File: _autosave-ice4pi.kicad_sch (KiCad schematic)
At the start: 32 parts, among them J1 Conn_02x03, J2 Raspberry_Pi_2_3, J3 USB_C_Receptacle_USB2.0, J5 RJ45_Abracon_ARJP11A-MASA-B-A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, U1 ENC28J60x-SS, U2 DSC1001DE1-025.0000, U3 TPS2375-1

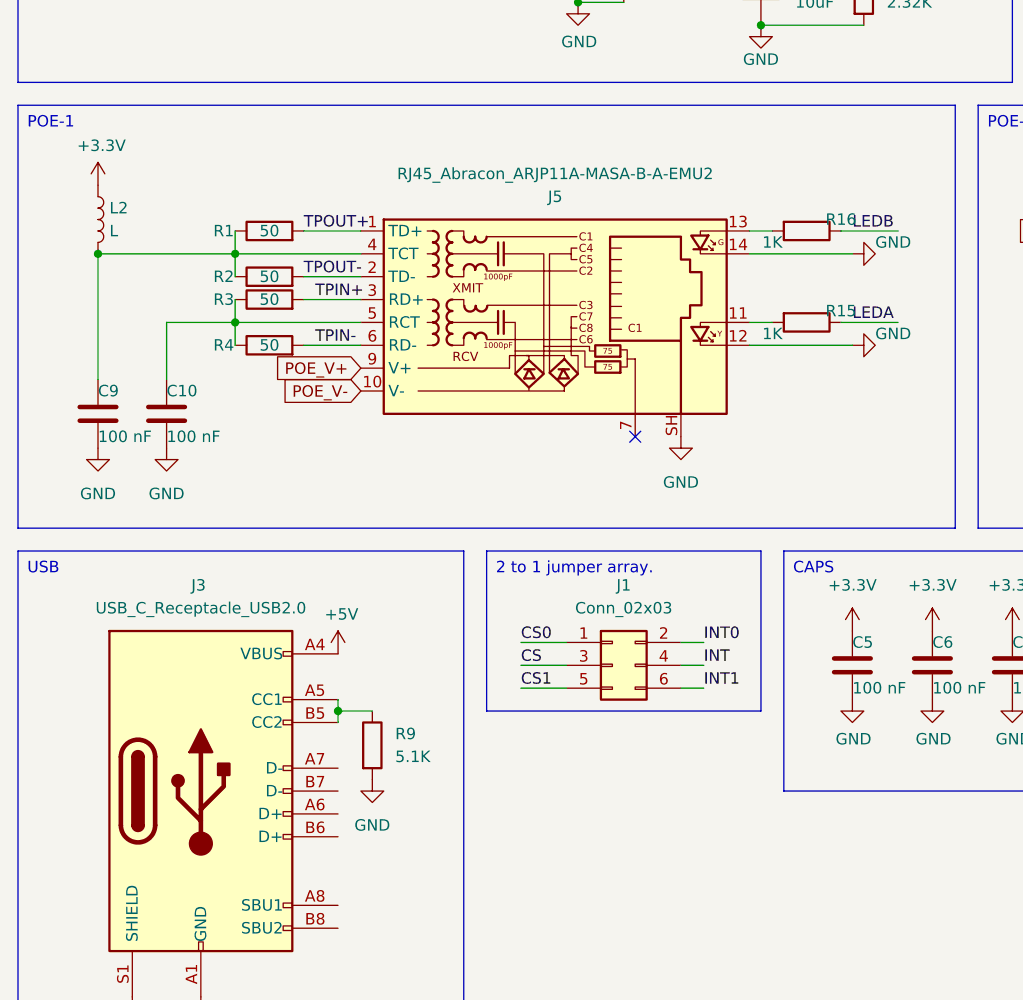
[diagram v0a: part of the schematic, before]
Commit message: feat: pos.csv
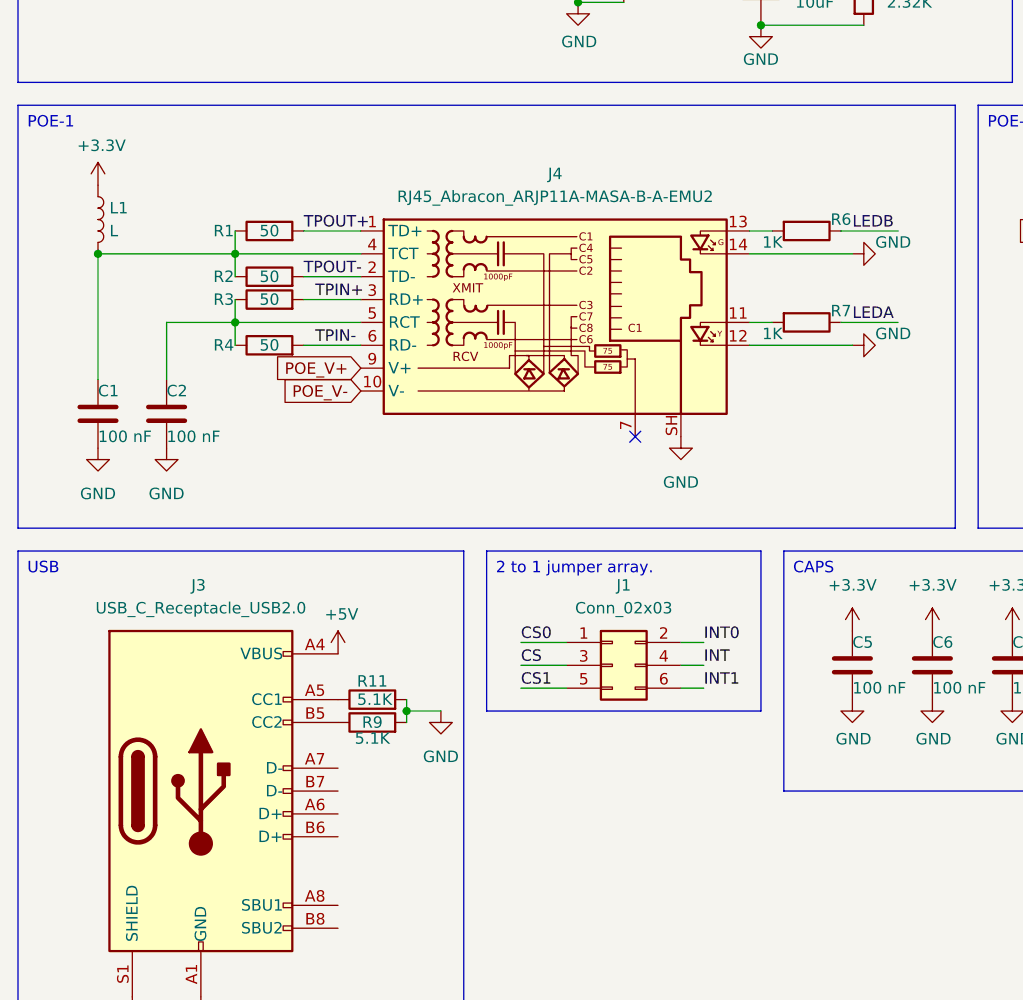
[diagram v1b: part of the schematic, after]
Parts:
- added R11: 5.1K, Resistor_SMD:R_0402_1005Metric, symbol Device:R
- renumbered C9 to C1, C10 to C2, J5 to J4, L2 to L1, R16 to R6, R15 to R7
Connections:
- net GND: now also R11.2
- net at J3.B5 (CC2), R9.1: no longer J3.A5 (CC1)
- new net: J3.A5 (CC1), R11.1
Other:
- moved on the sheet: R9
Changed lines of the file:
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@@
 	)
 	(junction
-		(at 50.8 149.86)
+		(at 137.16 45.72)
 		(diameter 0)
 		(color 0 0 0 0)
 	)
 	(junction
-		(at 137.16 45.72)
+		(at 157.48 96.52)
 		(diameter 0)
 		(color 0 0 0 0)
 	)
 	(junction
-		(at 157.48 96.52)
+		(at 39.37 106.68)
 		(diameter 0)
 		(color 0 0 0 0)
 	)
 	(junction
-		(at 39.37 106.68)
+		(at 58.42 149.86)
 		(diameter 0)
 		(color 0 0 0 0)
@@
 	(wire
 		(pts
-			(xy 137.16 43.18) (xy 137.16 45.72)
+			(xy 58.42 149.86) (xy 62.23 149.86)
 		)
 		(stroke
@@
 	(wire
 		(pts
-			(xy 31.75 40.64) (xy 39.37 40.64)
+			(xy 137.16 43.18) (xy 137.16 45.72)
 		)
 		(stroke
@@
 	(wire
 		(pts
-			(xy 71.12 144.78) (xy 76.2 144.78)
+			(xy 31.75 40.64) (xy 39.37 40.64)
 		)
 		(stroke
@@
 	(wire
 		(pts
-			(xy 96.52 106.68) (xy 99.06 106.68)
+			(xy 71.12 144.78) (xy 76.2 144.78)
 		)
 		(stroke
@@
 	(wire
 		(pts
-			(xy 50.8 149.86) (xy 50.8 151.13)
+			(xy 96.52 106.68) (xy 99.06 106.68)
 		)
 		(stroke
@@
 	(wire
 		(pts
-			(xy 50.8 148.59) (xy 50.8 149.86)
-		)
-		(stroke
-			(width 0)
-			(type default)
-		)
-	)
-	(wire
-		(pts
 			(xy 157.48 116.84) (xy 167.64 116.84)
 		)
@@
 	(wire
 		(pts
+			(xy 58.42 149.86) (xy 58.42 151.13)
+		)
+		(stroke
+			(width 0)
+			(type default)
+		)
+	)
+	(wire
+		(pts
 			(xy 96.52 96.52) (xy 99.06 96.52)
 		)
@@
 	(wire
 		(pts
-			(xy 167.64 106.68) (xy 167.64 111.76)
+			(xy 58.42 148.59) (xy 58.42 149.86)
 		)
 		(stroke
@@
 	(wire
 		(pts
-			(xy 97.79 45.72) (xy 101.6 45.72)
+			(xy 167.64 106.68) (xy 167.64 111.76)
 		)
 		(stroke
@@
 	(wire
 		(pts
-			(xy 167.64 96.52) (xy 185.42 96.52)
+			(xy 97.79 45.72) (xy 101.6 45.72)
 		)
 		(stroke
@@
 	(wire
 		(pts
-			(xy 31.75 106.68) (xy 31.75 113.03)
+			(xy 167.64 96.52) (xy 185.42 96.52)
 		)
 		(stroke
@@
 	(wire
 		(pts
-			(xy 142.24 96.52) (xy 142.24 104.14)
+			(xy 31.75 106.68) (xy 31.75 113.03)
 		)
 		(stroke
@@
 	(wire
 		(pts
-			(xy 50.8 149.86) (xy 54.61 149.86)
+			(xy 142.24 96.52) (xy 142.24 104.14)
 		)
 		(stroke
@@
 	)
 	(symbol
+		(lib_id "Device:R")
+		(at 54.61 148.59 90)
+		(unit 1)
+		(exclude_from_sim no)
+		(in_bom yes)
+		(on_board yes)
+		(dnp no)
+		(property "Reference" "R11"
+			(at 54.61 146.558 90)
+			(effects
+				(font
+					(size 1.27 1.27)
+				)
+			)
+		)
+		(property "Value" "5.1K"
+			(at 54.864 148.59 90)
+			(effects
+				(font
+					(size 1.27 1.27)
+				)
+			)
+		)
+		(property "Footprint" "Resistor_SMD:R_0402_1005Metric"
+			(at 54.61 150.368 90)
+			(effects
+				(font
+					(size 1.27 1.27)
+				)
+				(hide yes)
+			)
+		)
+		(property "Datasheet" "~"
+			(at 54.61 148.59 0)
+			(effects
+				(font
+					(size 1.27 1.27)
+				)
+				(hide yes)
+			)
+		)
+		(property "Description" ""
+			(at 54.61 148.59 0)
+			(effects
+				(font
+					(size 1.27 1.27)
+				)
+				(hide yes)
+			)
+		)
+		(pin "1"
+		)
+		(pin "2"
+		)
+		(instances
+			(project "ice4pi"
+				(path "/0f54db53-a272-4955-88fb-d7ab00657bb0"
+					(reference "R11")
+					(unit 1)
+				)
+			)
+		)
+	)
+	(symbol
 		(lib_id "power:+3.3V")
 		(at 24.13 91.44 0)
@@
 	(symbol
 		(lib_id "Device:R")
-		(at 54.61 153.67 0)
+		(at 54.61 151.13 90)
 		(unit 1)
 		(exclude_from_sim no)
@@
 		(on_board yes)
 		(dnp no)
-		(fields_autoplaced yes)
 		(property "Reference" "R9"
-			(at 57.15 152.3999 0)
+			(at 54.61 151.13 90)
 			(effects
 				(font
 					(size 1.27 1.27)
 				)
-				(justify left)
 			)
 		)
 		(property "Value" "5.1K"
-			(at 57.15 154.9399 0)
+			(at 54.61 152.908 90)
 			(effects
 				(font
 					(size 1.27 1.27)
 				)
-				(justify left)
 			)
 		)
 		(property "Footprint" "Resistor_SMD:R_0402_1005Metric"
-			(at 52.832 153.67 90)
+			(at 54.61 152.908 90)
 			(effects
 				(font
@@
 		)
 		(property "Datasheet" "~"
-			(at 54.61 153.67 0)
+			(at 54.61 151.13 0)
 			(effects
 				(font
@@
 		)
 		(property "Description" ""
-			(at 54.61 153.67 0)
+			(at 54.61 151.13 0)
 			(effects
 				(font
@@
 		(on_board yes)
 		(dnp no)
-		(property "Reference" "C9"
+		(property "Reference" "C1"
 			(at 24.13 114.3 0)
 			(effects
@@
 			(project "ice4pi"
 				(path "/0f54db53-a272-4955-88fb-d7ab00657bb0"
-					(reference "C9")
+					(reference "C1")
 					(unit 1)
 				)
@@
 		(on_board yes)
 		(dnp no)
-		(property "Reference" "C10"
+		(property "Reference" "C2"
 			(at 31.75 114.3 0)
 			(effects
@@
 			(project "ice4pi"
 				(path "/0f54db53-a272-4955-88fb-d7ab00657bb0"
-					(reference "C10")
+					(reference "C2")
 					(unit 1)
 				)
@@
 		(dnp no)
 		(fields_autoplaced yes)
-		(property "Reference" "L2"
+		(property "Reference" "L1"
 			(at 25.4 93.9799 0)
 			(effects
@@
 			(project "ice4pi"
 				(path "/0f54db53-a272-4955-88fb-d7ab00657bb0"
-					(reference "L2")
+					(reference "L1")
 					(unit 1)
 				)
@@
 		(dnp no)
 		(fields_autoplaced yes)
-		(property "Reference" "J5"
-			(at 74.93 92.71 0)
+		(property "Reference" "J4"
+			(at 74.93 90.17 0)
 			(effects
 				(font
@@
 		)
 		(property "Value" "RJ45_Abracon_ARJP11A-MASA-B-A-EMU2"
-			(at 74.93 90.17 0)
+			(at 74.93 92.71 0)
 			(effects
 				(font
@@
 			(project ""
 				(path "/0f54db53-a272-4955-88fb-d7ab00657bb0"
-					(reference "J5")
+					(reference "J4")
 					(unit 1)
 				)
@@
 		(on_board yes)
 		(dnp no)
-		(property "Reference" "R15"
+		(property "Reference" "R7"
 			(at 106.68 105.41 90)
 			(effects
@@
 			(project "ice4pi"
 				(path "/0f54db53-a272-4955-88fb-d7ab00657bb0"
-					(reference "R15")
+					(reference "R7")
 					(unit 1)
 				)
@@
 		(on_board yes)
 		(dnp no)
-		(property "Reference" "R16"
+		(property "Reference" "R6"
 			(at 106.68 95.25 90)
 			(effects
@@
 			(project "ice4pi"
 				(path "/0f54db53-a272-4955-88fb-d7ab00657bb0"
-					(reference "R16")
+					(reference "R6")
 					(unit 1)
 				)
@@
 	(symbol
 		(lib_id "power:GND")
-		(at 54.61 157.48 0)
+		(at 62.23 149.86 0)
 		(unit 1)
 		(exclude_from_sim no)
@@
 		(fields_autoplaced yes)
 		(property "Reference" "#PWR0112"
-			(at 54.61 163.83 0)
+			(at 62.23 156.21 0)
 			(effects
 				(font
@@
 		)
 		(property "Value" "GND"
-			(at 54.61 162.56 0)
+			(at 62.23 154.94 0)
 			(effects
 				(font
@@
 		)
 		(property "Footprint" ""
-			(at 54.61 157.48 0)
+			(at 62.23 149.86 0)
 			(effects
 				(font
@@
 		)
 		(property "Datasheet" ""
-			(at 54.61 157.48 0)
+			(at 62.23 149.86 0)
 			(effects
 				(font
@@
 		)
 		(property "Description" ""
-			(at 54.61 157.48 0)
+			(at 62.23 149.86 0)
 			(effects
 				(font
